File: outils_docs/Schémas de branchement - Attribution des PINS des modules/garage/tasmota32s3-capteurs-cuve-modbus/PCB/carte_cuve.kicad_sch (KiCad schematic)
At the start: 48 parts, among them J1 Entree 12 V, J10 Voie A0 (+12V / entree / GND), J11 Voie A1 (+12V / entree / GND), J12 Voie A2 (+12V / entree / GND), J13 Voie A3 (+12V / entree / GND), J14 Extension GPIO (3V3 GND 7 15 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, J4 Module ADS1115, J5 Module RS485 auto (VCC TX RX 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, J7 DS18B20 (3V3 / DQ / GND), J8 Ruban WS2815 (DI / BI / GND), J9 Extension I2C (3V3 GND SCL SD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, U1 TSR 1-2450, U3 74AHCT125

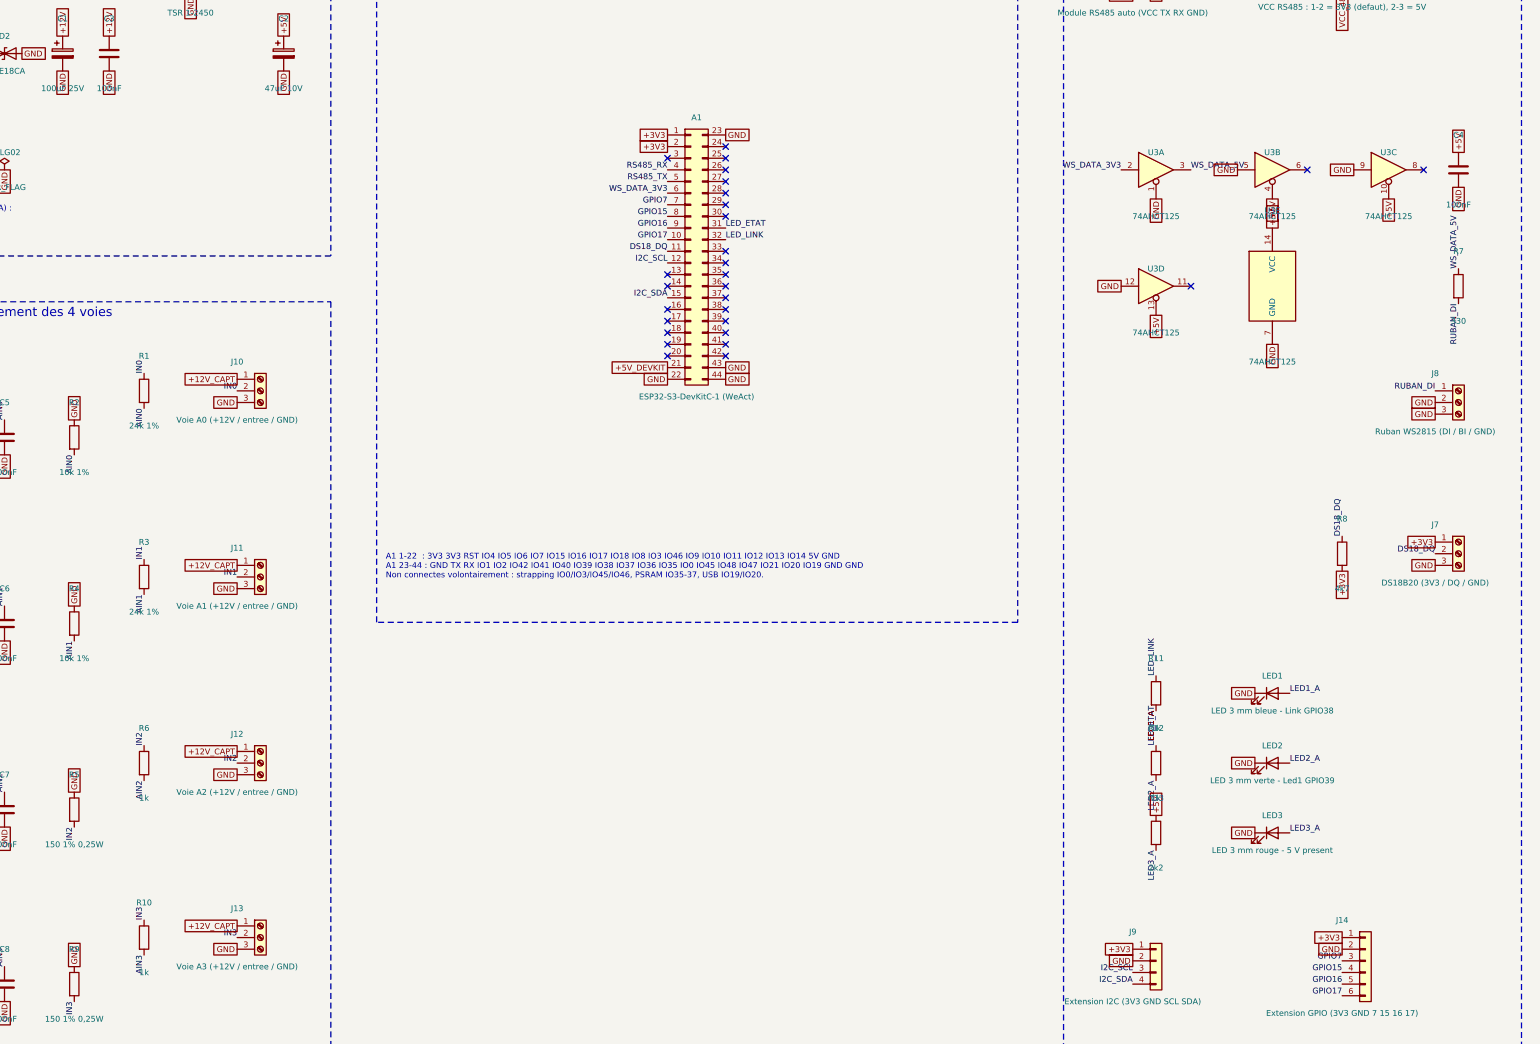
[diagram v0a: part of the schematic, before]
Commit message: feat: carte cuve v0.2, filtre du bouton du ruban et placement corrige
Bouton du ruban sur GPIO7 (J14 broche 3, cable > 1 m) : R14 rappel
10 k vers 3V3, R15 1 k serie, C9 100 nF vers 0V.

Placement : les 9 erreurs DRC de la v0.1 (D1 et U1 sous le DevKit,
R11-R13 sous l'ADS1115) sont corrigees. D1 au-dessus du DevKit ;
U1, C1, C2 regroupes entre R7 et l'ADS1115, C3 colle sous U1 (boucle
d'entree 3,65 mm) ; F1 hors du trajet des cables USB-C ; R11-R13
debout, LED au pas de 6,35 ; R11 180 ohm (bleue), R12 560 ohm (verte).

Masses des LED et de C9/J14 routees avant les signaux : C9 et J14.2
formaient un ilot sans lien avec la masse.

DRC avec parite : 0 violation, 0 non connecte, 0 ecart ; ERC 0 erreur.
Avant commande : identifier le module RS485, mesurer le DevKit et les
modules, verifier la hauteur des fusibles rearmables.
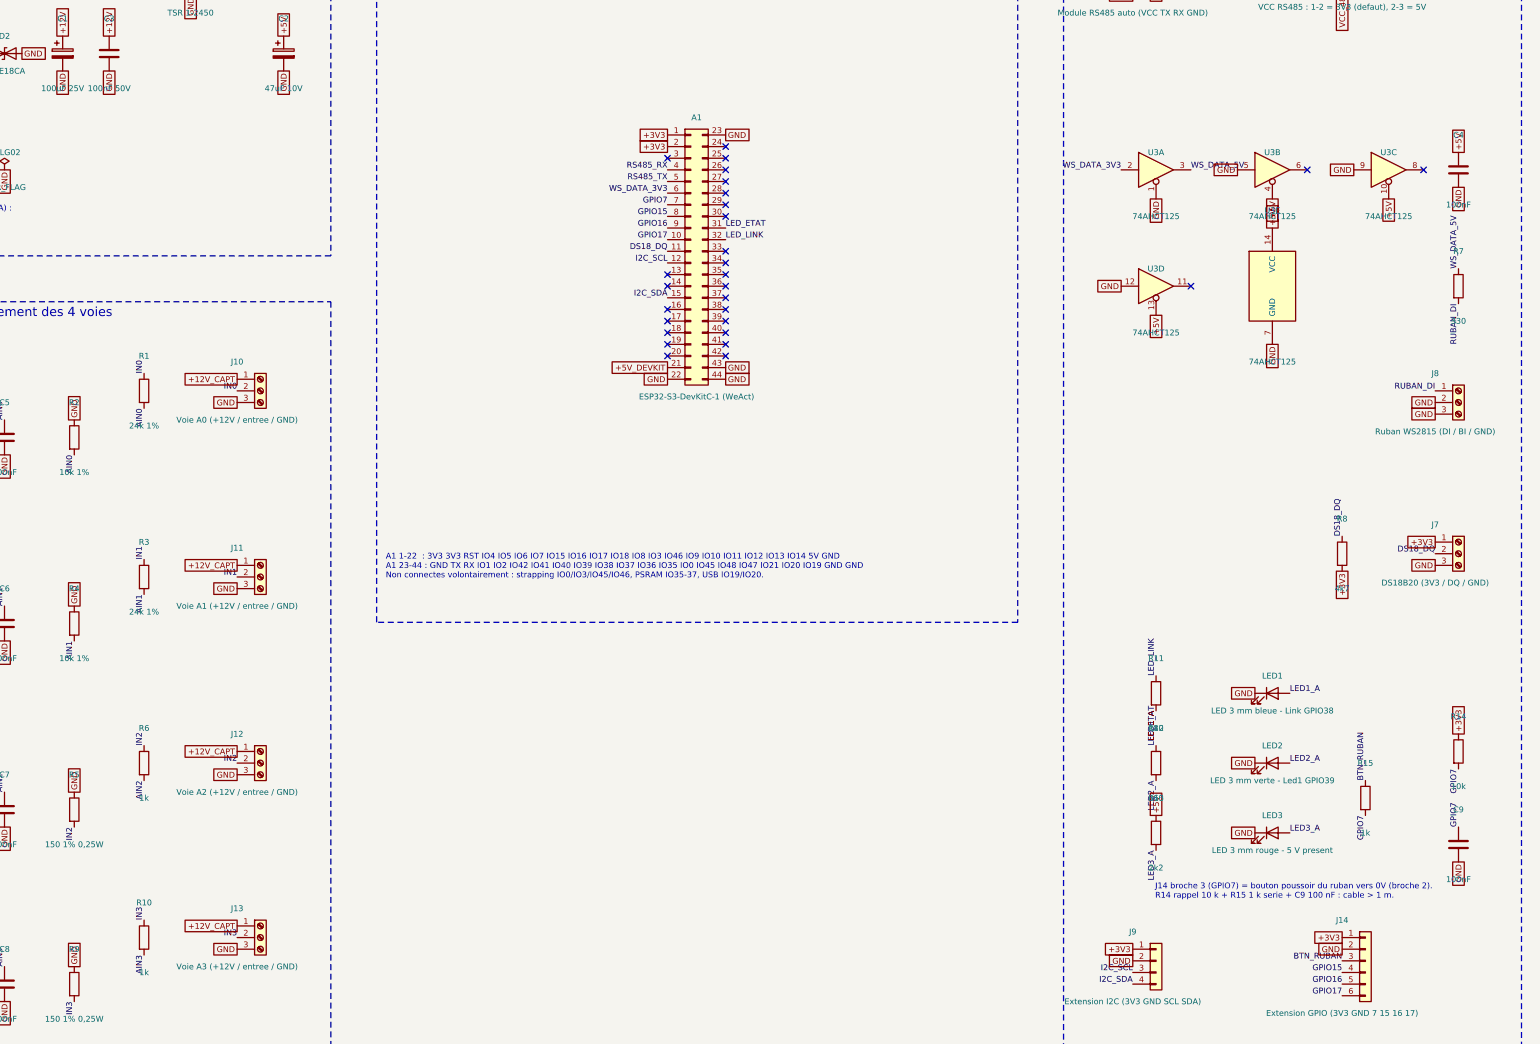
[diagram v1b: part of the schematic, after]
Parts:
- added C9: 100nF, Capacitor_THT:C_Disc_D5.0mm_W2.5mm_P5.00mm, symbol Device:C
- added R14: 10k, Resistor_THT:R_Axial_DIN0207_L6.3mm_D2.5mm_P10.16mm_Horizontal, symbol Device:R
- added R15: 1k, Resistor_THT:R_Axial_DIN0207_L6.3mm_D2.5mm_P2.54mm_Vertical, symbol Device:R
- C3: value 100nF -> 100nF 50V; footprint Capacitor_THT:C_Disc_D5.0mm_W2.5mm_P5.00mm -> Capacitor_THT:C_Disc_D3.0mm_W1.6mm_P2.50mm
- R11: value 1k -> 180; footprint Resistor_THT:R_Axial_DIN0207_L6.3mm_D2.5mm_P10.16mm_Horizontal -> Resistor_THT:R_Axial_DIN0207_L6.3mm_D2.5mm_P2.54mm_Vertical
- R12: value 1k -> 560; footprint Resistor_THT:R_Axial_DIN0207_L6.3mm_D2.5mm_P10.16mm_Horizontal -> Resistor_THT:R_Axial_DIN0207_L6.3mm_D2.5mm_P2.54mm_Vertical
- R13: footprint Resistor_THT:R_Axial_DIN0207_L6.3mm_D2.5mm_P10.16mm_Horizontal -> Resistor_THT:R_Axial_DIN0207_L6.3mm_D2.5mm_P2.54mm_Vertical
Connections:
- net +3V3: now also R14.1
- net GND: now also C9.2
- net GPIO7: now also C9.1, R14.2, R15.2; no longer J14.3 (Pin_3)
- new net BTN_RUBAN: J14.3 (Pin_3), R15.1
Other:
- note added: "J14 broche 3 (GPIO7) = bouton poussoir du ruban vers 0V (broche 2). R14 rappel 10 k + R15 1 k serie + C9 100 nF : cable > 1 m."

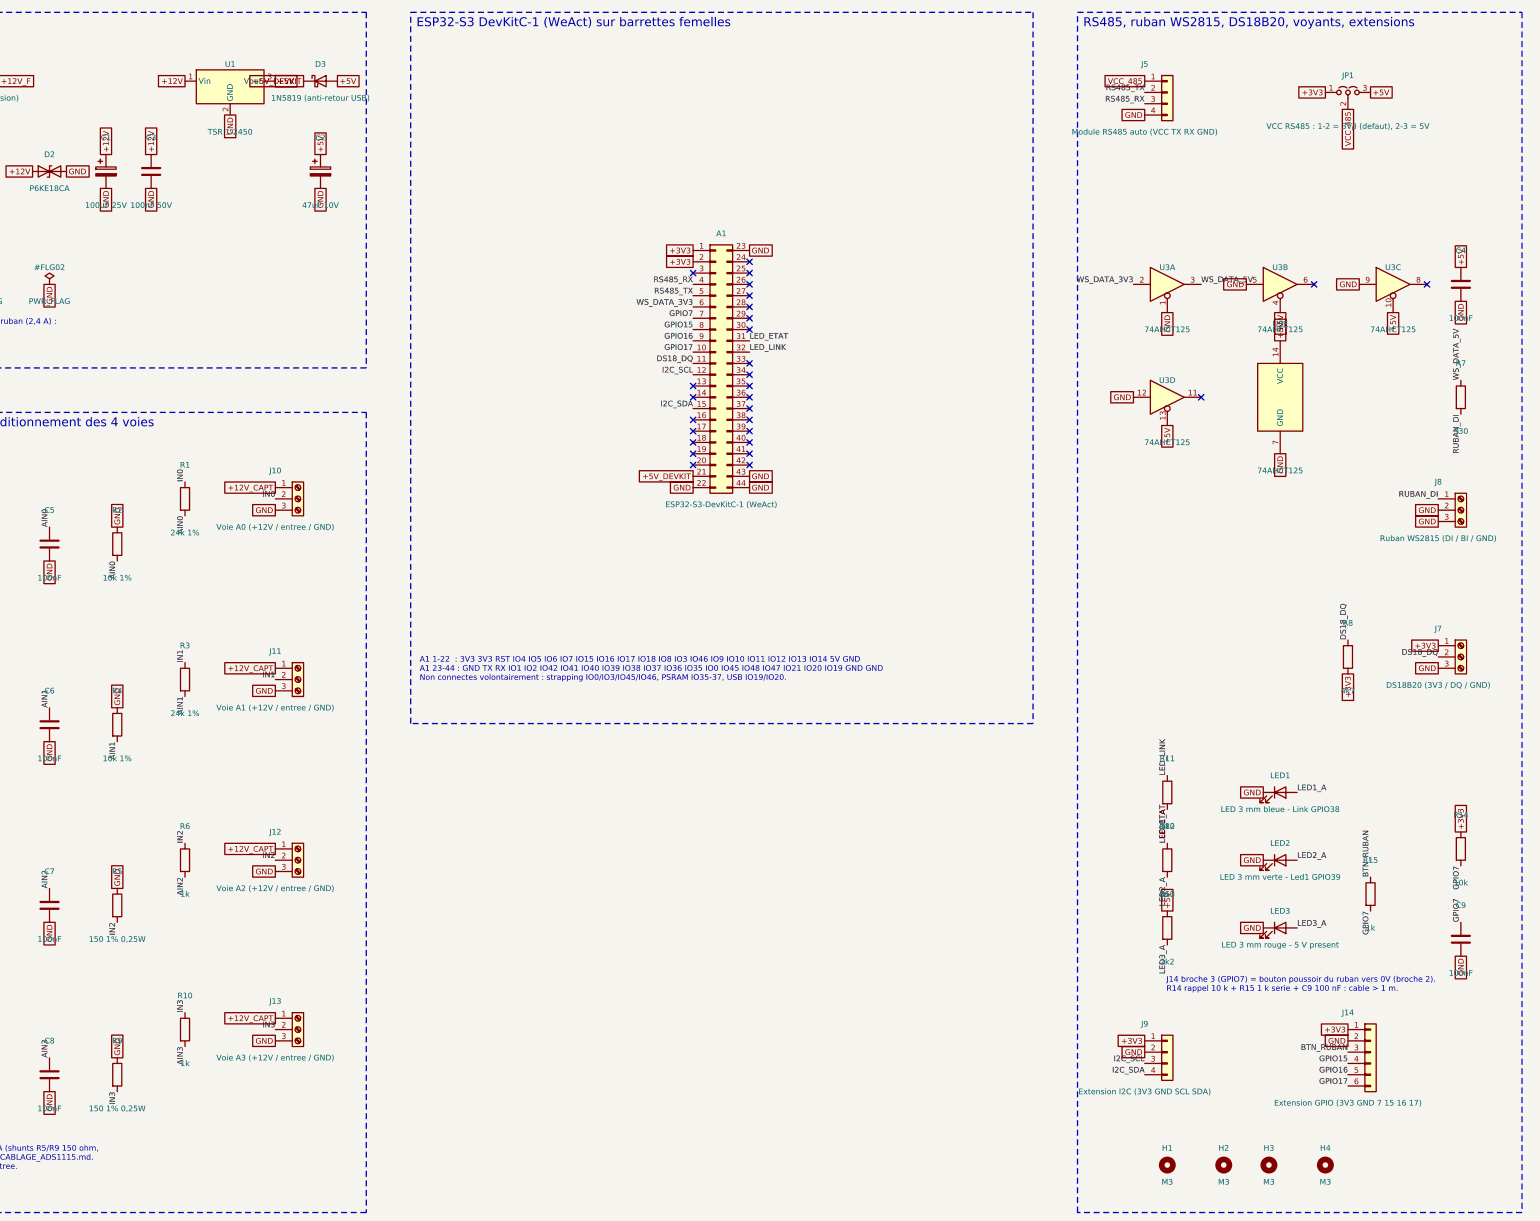
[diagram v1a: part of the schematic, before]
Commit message: feat(pcb): carte cuve v0.3, module RS485 XY-017 reel et corrections de la relecture
- Module RS485 XY-017 (confirme) avec son empreinte Modules_Tasmota, debout
  sous le DevKit ; bornier A/B au-dessus du coin bas droit, libere en
  decalant les 4 voies analogiques de 10,16 mm a gauche.
- JP1 supprime : RS485 en 3,3 V fixe (en 5 V, son RXD mettait 5 V sur GPIO4).
- Bornier a vis J15 pour le bouton du ruban (cable > 1 m).
- Voies dans l'ordre entree / 0V / +12 : un brin entre bornes voisines ne
  brule plus le shunt ; type de voie (0-10V, 4-20mA) serigraphie.
- R16 10 k de rappel sur l'entree du 74AHCT125, C1 en 35 V, R8 debout.
- DRC parite 0, 0 non connecte, 0 violation ; ERC 0 erreur ; masse en 1 groupe.
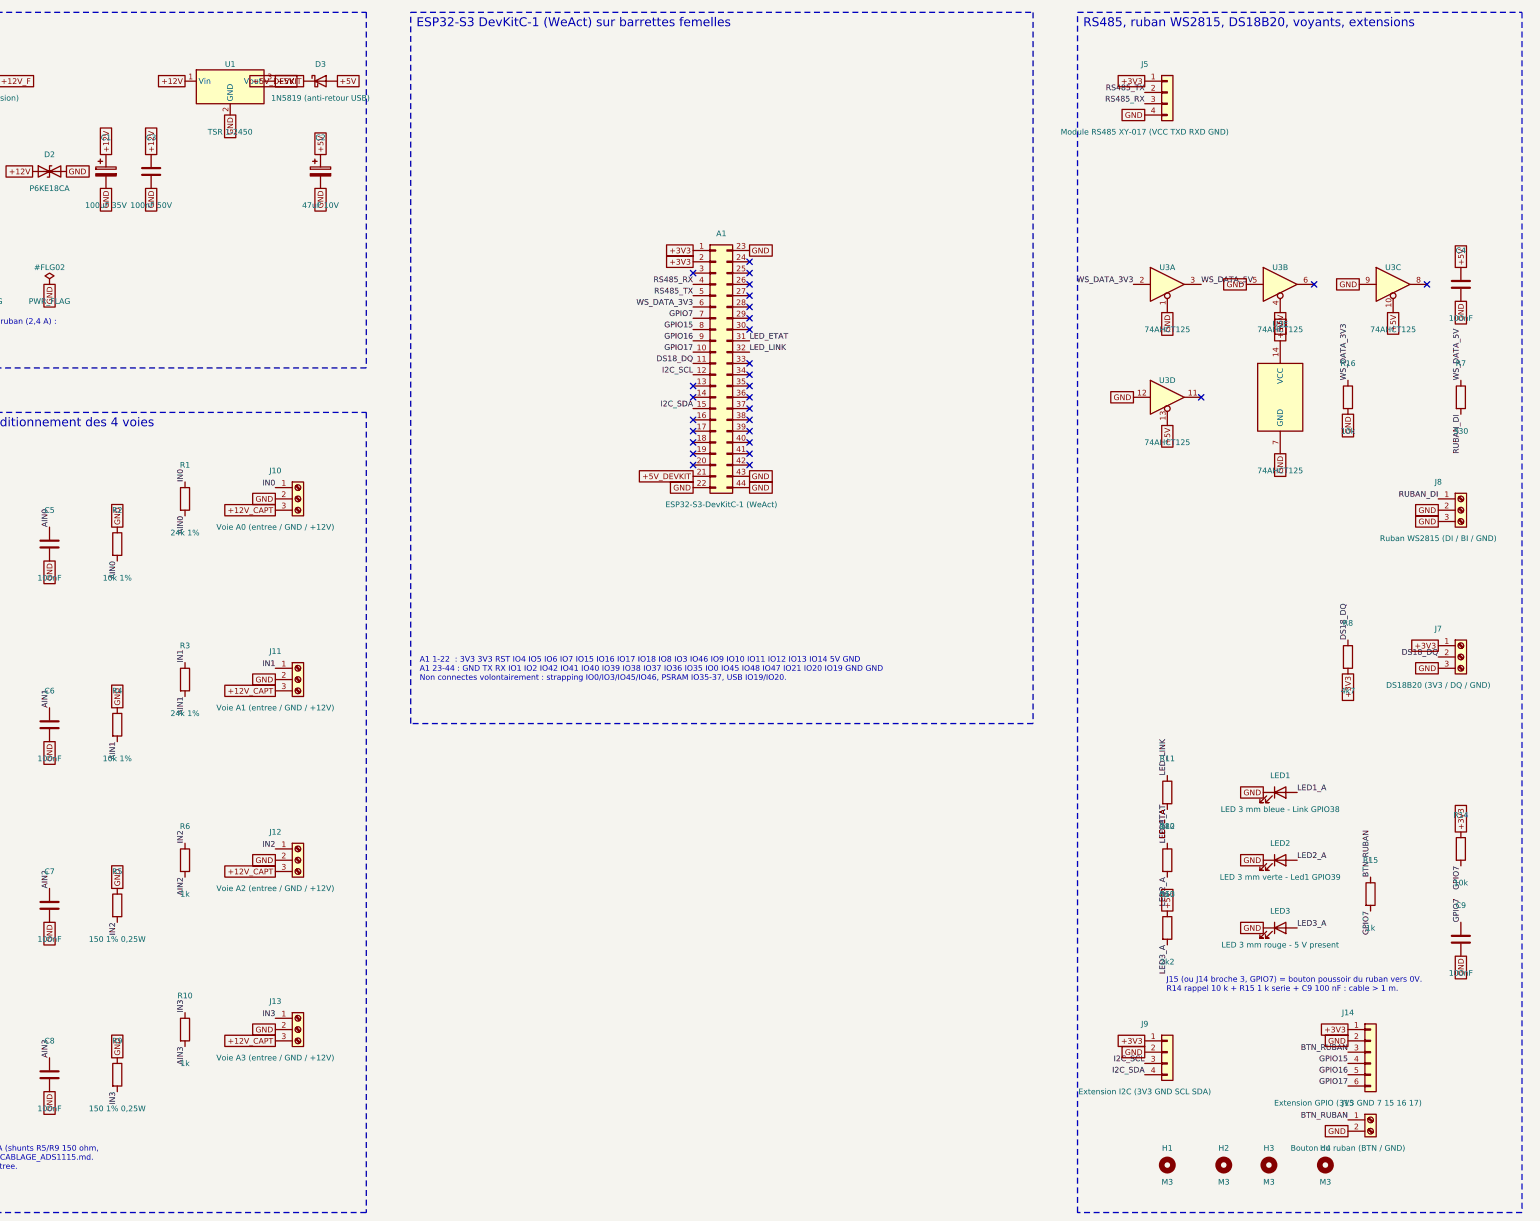
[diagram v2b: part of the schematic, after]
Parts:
- removed JP1: VCC RS485 : 1-2 = 3V3 (defaut), 2-3 = 5V, Connector_PinHeader_2.54mm:PinHeader_1x03_P2.54mm_Vertical, symbol Jumper:Jumper_3_Open
- added J15: Bouton du ruban (BTN / GND), TerminalBlock_Phoenix:TerminalBlock_Phoenix_MKDS-1,5-2-5.08_1x02_P5.08mm_Horizontal, symbol Connector:Screw_Terminal_01x02
- added R16: 10k, Resistor_THT:R_Axial_DIN0207_L6.3mm_D2.5mm_P2.54mm_Vertical, symbol Device:R
- C1: value 100uF 25V -> 100uF 35V
- J10: value Voie A0 (+12V / entree / GND) -> Voie A0 (entree / GND / +12V)
- J11: value Voie A1 (+12V / entree / GND) -> Voie A1 (entree / GND / +12V)
- J12: value Voie A2 (+12V / entree / GND) -> Voie A2 (entree / GND / +12V)
- J13: value Voie A3 (+12V / entree / GND) -> Voie A3 (entree / GND / +12V)
- J5: value Module RS485 auto (VCC TX RX GND) -> Module RS485 XY-017 (VCC TXD RXD GND); footprint Connector_PinSocket_2.54mm:PinSocket_1x04_P2.54mm_Vertical -> Modules_Tasmota:Module_RS485_Auto_XY-017
- R8: footprint Resistor_THT:R_Axial_DIN0207_L6.3mm_D2.5mm_P10.16mm_Horizontal -> Resistor_THT:R_Axial_DIN0207_L6.3mm_D2.5mm_P2.54mm_Vertical
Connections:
- net VCC_485 is gone; now on net +3V3: J5.1 (Pin_1)
- net +12V_CAPT: now also J10.3 (Pin_3), J11.3 (Pin_3), J12.3 (Pin_3), J13.3 (Pin_3); no longer J10.1 (Pin_1), J11.1 (Pin_1), J12.1 (Pin_1), J13.1 (Pin_1)
- net BTN_RUBAN: now also J15.1 (Pin_1)
- net GND: now also J10.2 (Pin_2), J11.2 (Pin_2), J12.2 (Pin_2), J13.2 (Pin_2), J15.2 (Pin_2), R16.2; no longer J10.3 (Pin_3), J11.3 (Pin_3), J12.3 (Pin_3), J13.3 (Pin_3)
- net IN0: now also J10.1 (Pin_1); no longer J10.2 (Pin_2)
- net IN1: now also J11.1 (Pin_1); no longer J11.2 (Pin_2)
- net IN2: now also J12.1 (Pin_1); no longer J12.2 (Pin_2)
- net IN3: now also J13.1 (Pin_1); no longer J13.2 (Pin_2)
- net WS_DATA_3V3: now also R16.1
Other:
- note added: "J15 (ou J14 broche 3, GPIO7) = bouton poussoir du ruban vers 0V. R14 rappel 10 k + R15 1 k serie + C9 100 nF : cable > 1 m."
- note removed: "J14 broche 3 (GPIO7) = bouton poussoir du ruban vers 0V (broche 2). R14 rappel 10 k + R15 1 k serie + C9 100 nF : cable > 1 m."
